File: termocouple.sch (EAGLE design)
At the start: 21 parts, among them IC1 MAX31855, IC2 MAX31855, U2 TC1262_VDB, X2 1751248, X3 1751248

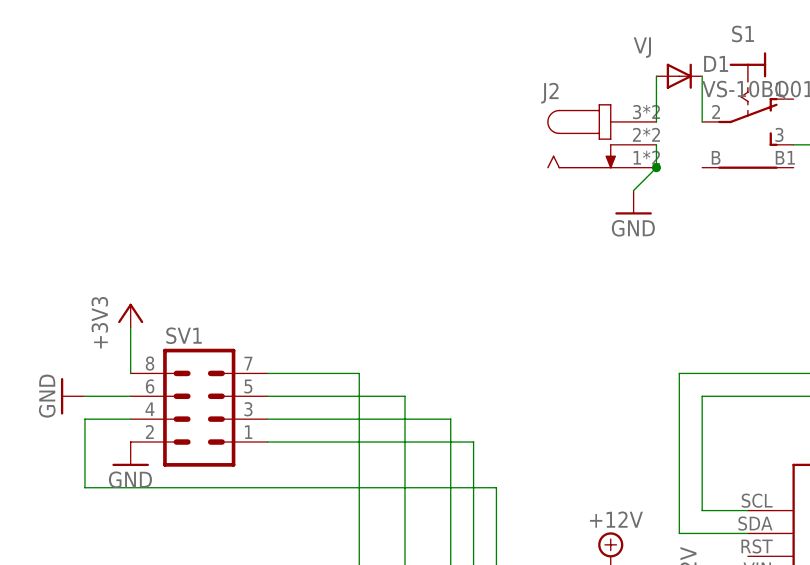
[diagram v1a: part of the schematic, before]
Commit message: pcb add fiducials
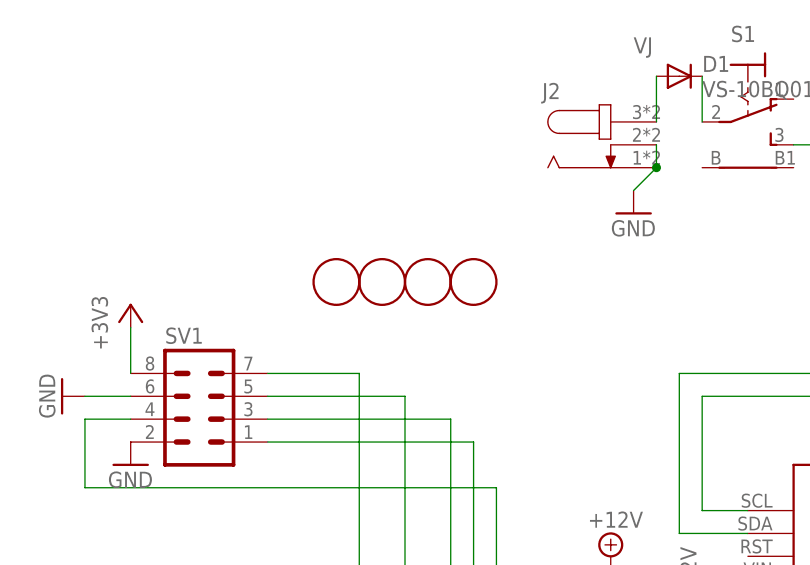
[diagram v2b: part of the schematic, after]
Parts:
- added U$4, U$5, U$6, U$7: FIDUCIAL, tracker:FIDUCIAL
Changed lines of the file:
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@@
 <part name="GND15" library="supply1" deviceset="GND" device=""/>
 <part name="GND16" library="supply1" deviceset="GND" device=""/>
+<part name="U$4" library="tracker" deviceset="FIDUCIAL" device=""/>
+<part name="U$5" library="tracker" deviceset="FIDUCIAL" device=""/>
+<part name="U$6" library="tracker" deviceset="FIDUCIAL" device=""/>
+<part name="U$7" library="tracker" deviceset="FIDUCIAL" device=""/>
 </parts>
 <sheets>
@@
 <instance part="GND15" gate="1" x="-17.78" y="17.78"/>
 <instance part="GND16" gate="1" x="-22.86" y="-12.7"/>
+<instance part="U$4" gate="G$1" x="12.7" y="81.28"/>
+<instance part="U$5" gate="G$1" x="17.78" y="81.28"/>
+<instance part="U$6" gate="G$1" x="22.86" y="81.28"/>
+<instance part="U$7" gate="G$1" x="27.94" y="81.28"/>
 </instances>
 <busses>
